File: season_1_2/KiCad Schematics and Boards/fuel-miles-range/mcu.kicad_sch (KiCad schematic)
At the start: 1 part, among them U602 STM32G0B1CET6N

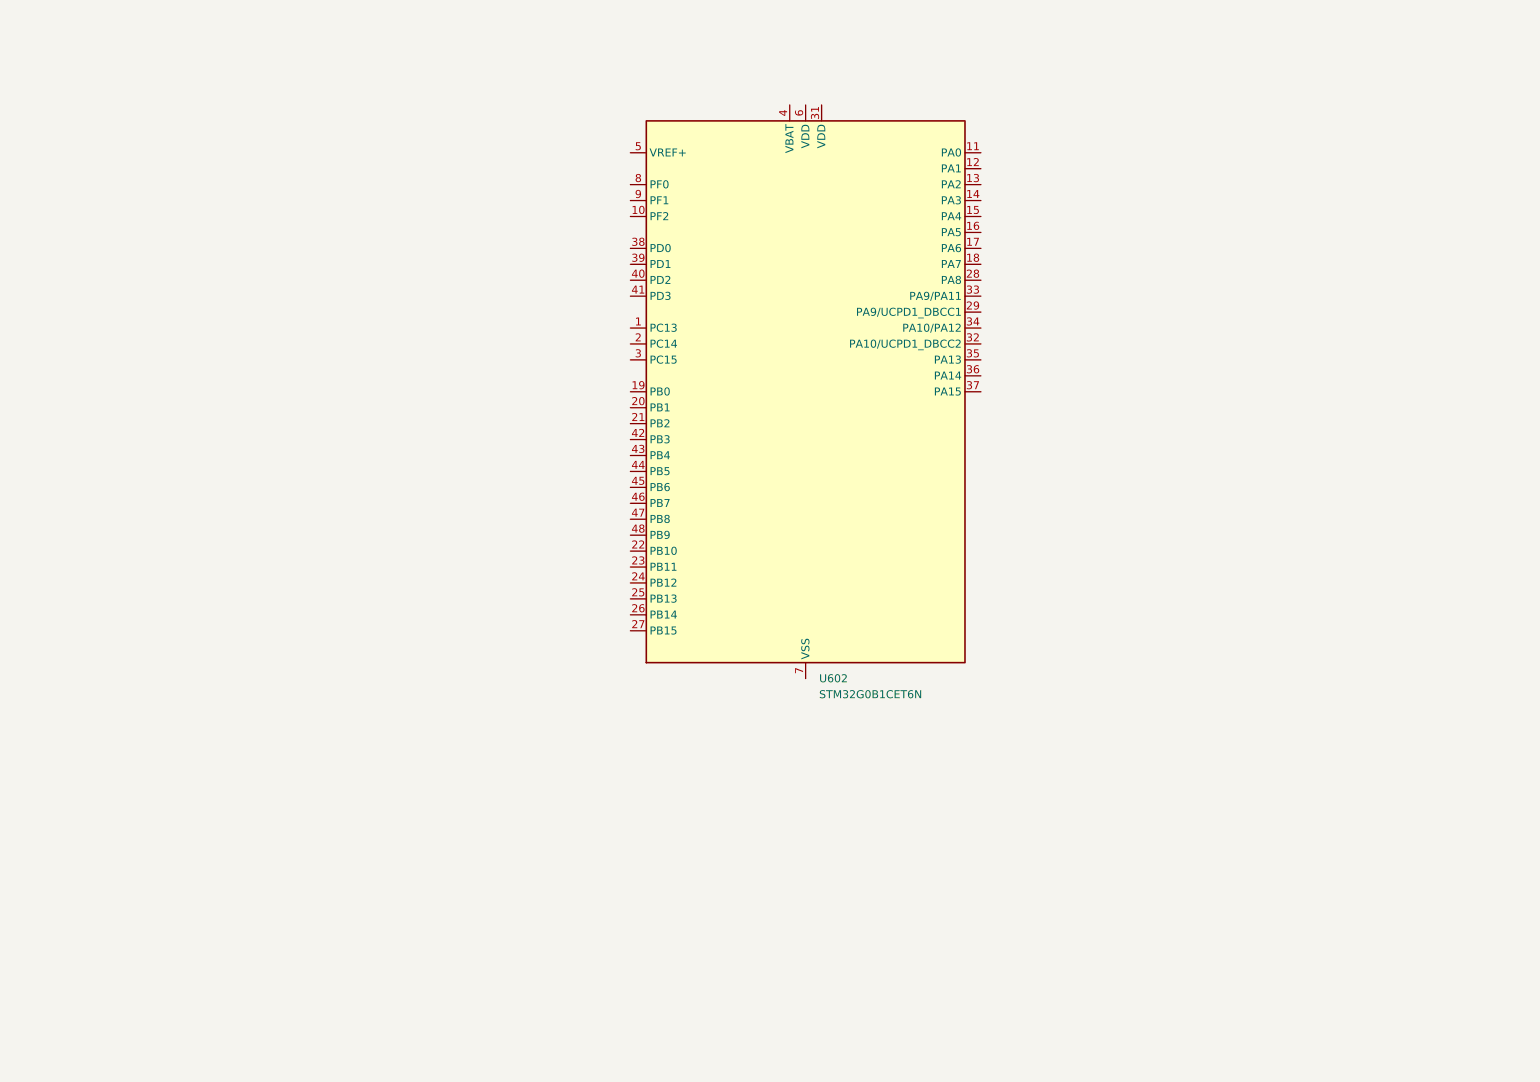
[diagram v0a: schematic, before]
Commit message: Added lots of electronic devices and routes
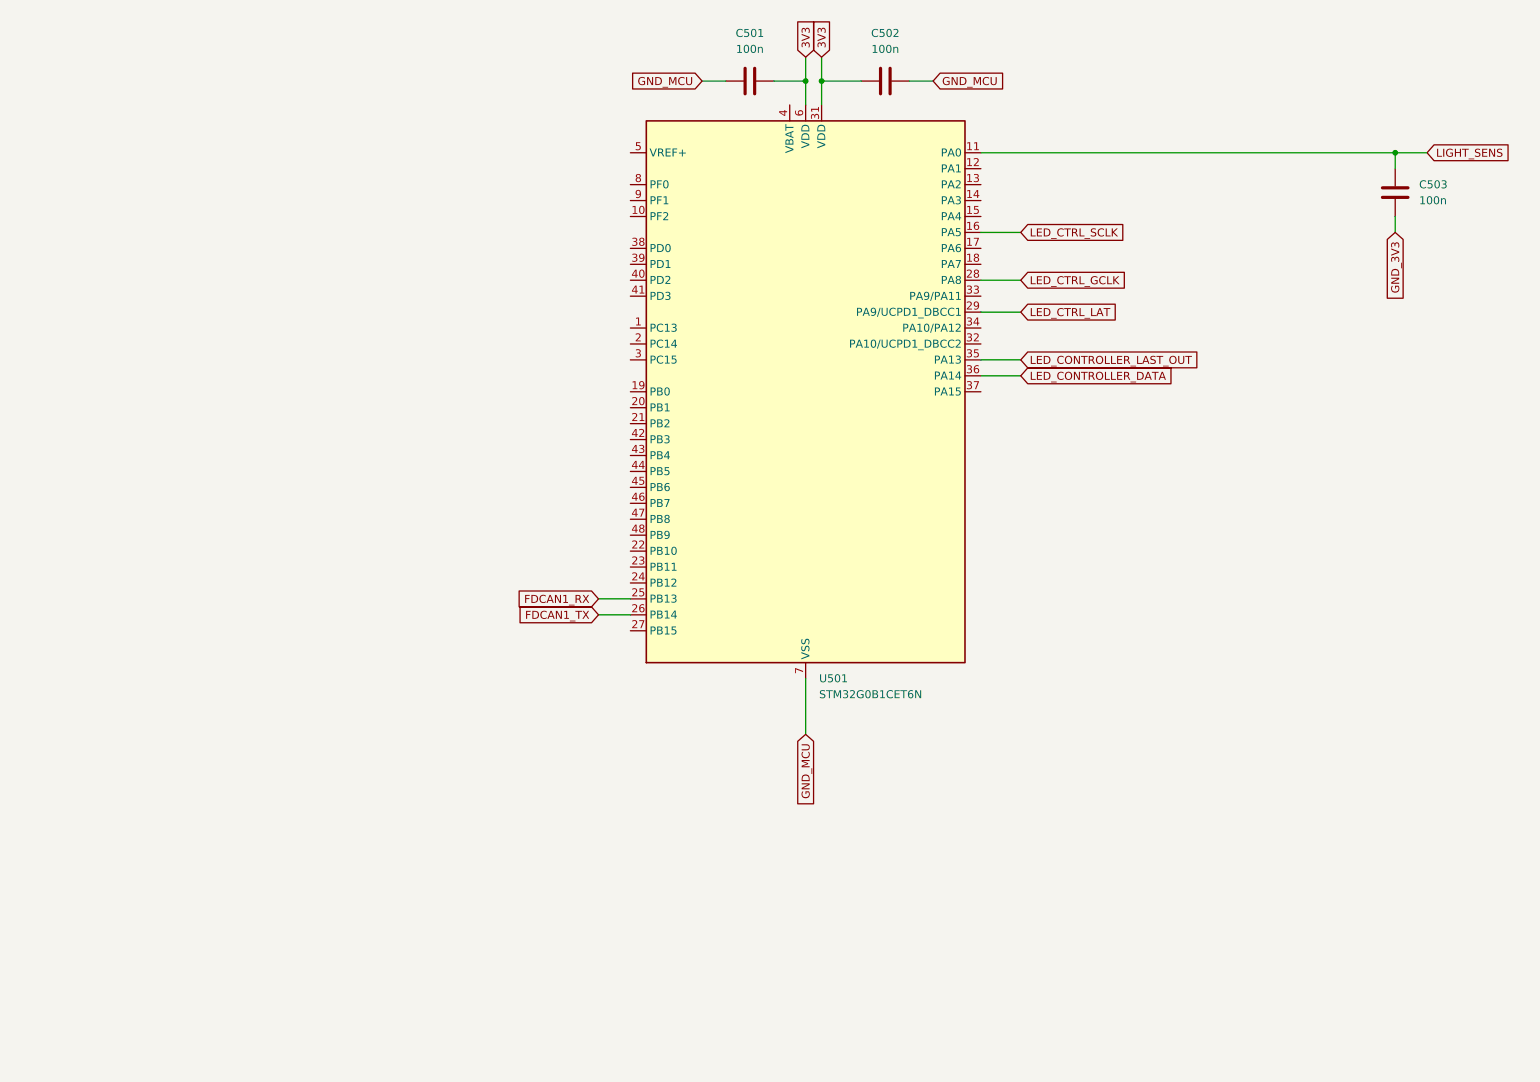
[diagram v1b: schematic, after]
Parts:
- added C501, C502, C503: 100n, Capacitor_SMD:C_1206_3216Metric, symbol Device:C
- renumbered U602 to U501
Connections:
- net LIGHT_SENS: now reaches U501.11 (PA0)
- net LIGHT_SENS: now also C503.1
- net LED_CTRL_SCLK: now reaches U501.16 (PA5)
- net FDCAN1_RX: now reaches U501.25 (PB13)
- net FDCAN1_TX: now reaches U501.26 (PB14)
- net LED_CTRL_GCLK: now reaches U501.28 (PA8)
- net LED_CTRL_LAT: now reaches U501.29 (PA9/UCPD1_DBCC1)
- net GND_MCU: now reaches U501.30 (VSS), U501.7 (VSS)
- net GND_MCU: now also C501.1, C502.1
- net 3V3: now reaches U501.31 (VDD)
- net 3V3: now also U501.6 (VDD), C501.2, C502.2
- net LED_CONTROLLER_LAST_OUT: now reaches U501.35 (PA13)
- net LED_CONTROLLER_DATA: now reaches U501.36 (PA14)
- new net GND_3V3: C503.2

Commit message: Added 4 missing wires for LED BAR 3, added programming PINs for STM32
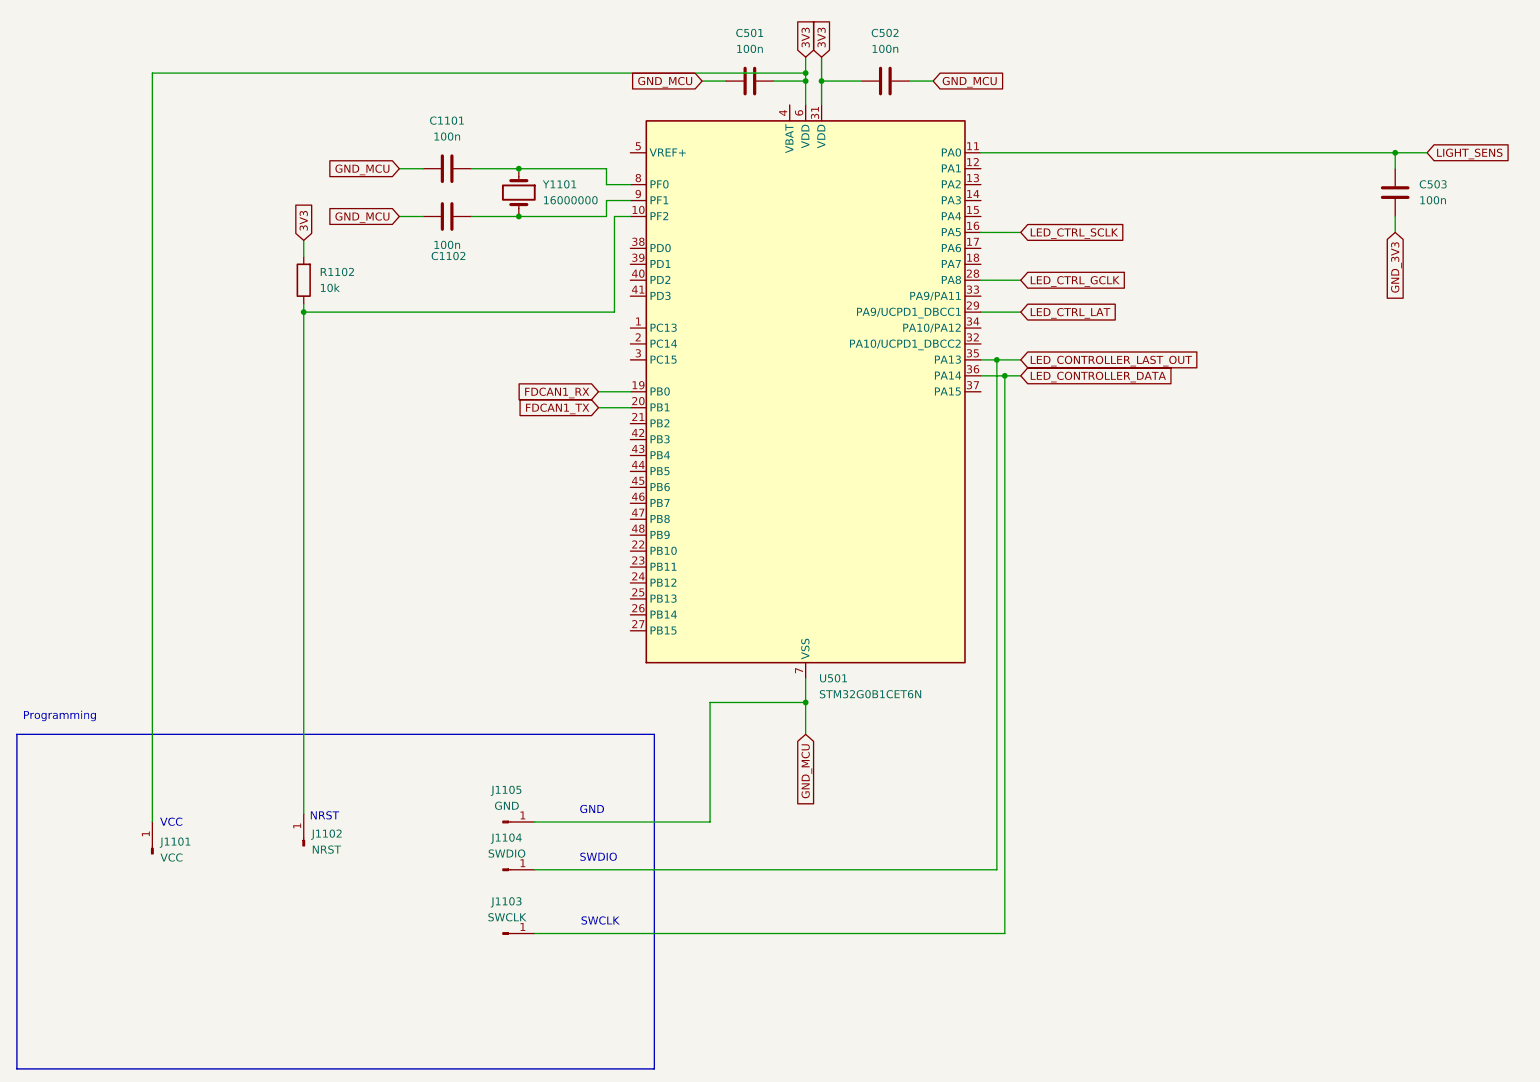
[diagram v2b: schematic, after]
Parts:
- added C1101, C1102: 100n, Capacitor_SMD:C_1206_3216Metric, symbol Device:C
- added J1101: VCC, TestPoint:TestPoint_Pad_4.0x4.0mm, symbol Connector:Conn_01x01_Pin
- added J1102: NRST, TestPoint:TestPoint_Pad_4.0x4.0mm, symbol Connector:Conn_01x01_Pin
- added J1103: SWCLK, TestPoint:TestPoint_Pad_4.0x4.0mm, symbol Connector:Conn_01x01_Pin
- added J1104: SWDIO, TestPoint:TestPoint_Pad_4.0x4.0mm, symbol Connector:Conn_01x01_Pin
- added J1105: GND, TestPoint:TestPoint_Pad_4.0x4.0mm, symbol Connector:Conn_01x01_Pin
- added R1102: 10k, Resistor_SMD:R_1206_3216Metric, symbol Device:R
- added Y1101: 16000000, Crystal:Crystal_SMD_ECS_CSM3X-2Pin_7.6x4.1mm, symbol Device:Crystal
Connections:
- net 3V3: now also J1101.1 (Pin_1), R1102.2
- net FDCAN1_RX: now also U501.19 (PB0); no longer U501.25 (PB13)
- net FDCAN1_TX: now also U501.20 (PB1); no longer U501.26 (PB14)
- net GND_MCU: now also C1101.1, C1102.1, J1105.1 (Pin_1)
- net LED_CONTROLLER_DATA: now also J1103.1 (Pin_1)
- net LED_CONTROLLER_LAST_OUT: now also J1104.1 (Pin_1)
- net at U501.10 (PF2): now also J1102.1 (Pin_1), R1102.1
- net at U501.8 (PF0): now also C1101.2, Y1101.1
- net at U501.9 (PF1): now also C1102.2, Y1101.2
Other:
- note added: "GND"
- note added: "NRST"
- note added: "Programming"
- note added: "SWCLK"
- note added: "SWDIO"
- note added: "VCC"
